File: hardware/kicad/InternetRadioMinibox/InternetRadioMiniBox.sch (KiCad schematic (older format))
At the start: 59 parts, among them IC1 ESP8266, IC2 ATMEGA328P-P, IC3 23K256, IC4 VS1011e, IC5 LM386, M1 TSR1-2433, M2 TSR1-2433, M3 TSR1-2433, P1 CONN_01X02, P2 CONN_01X02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

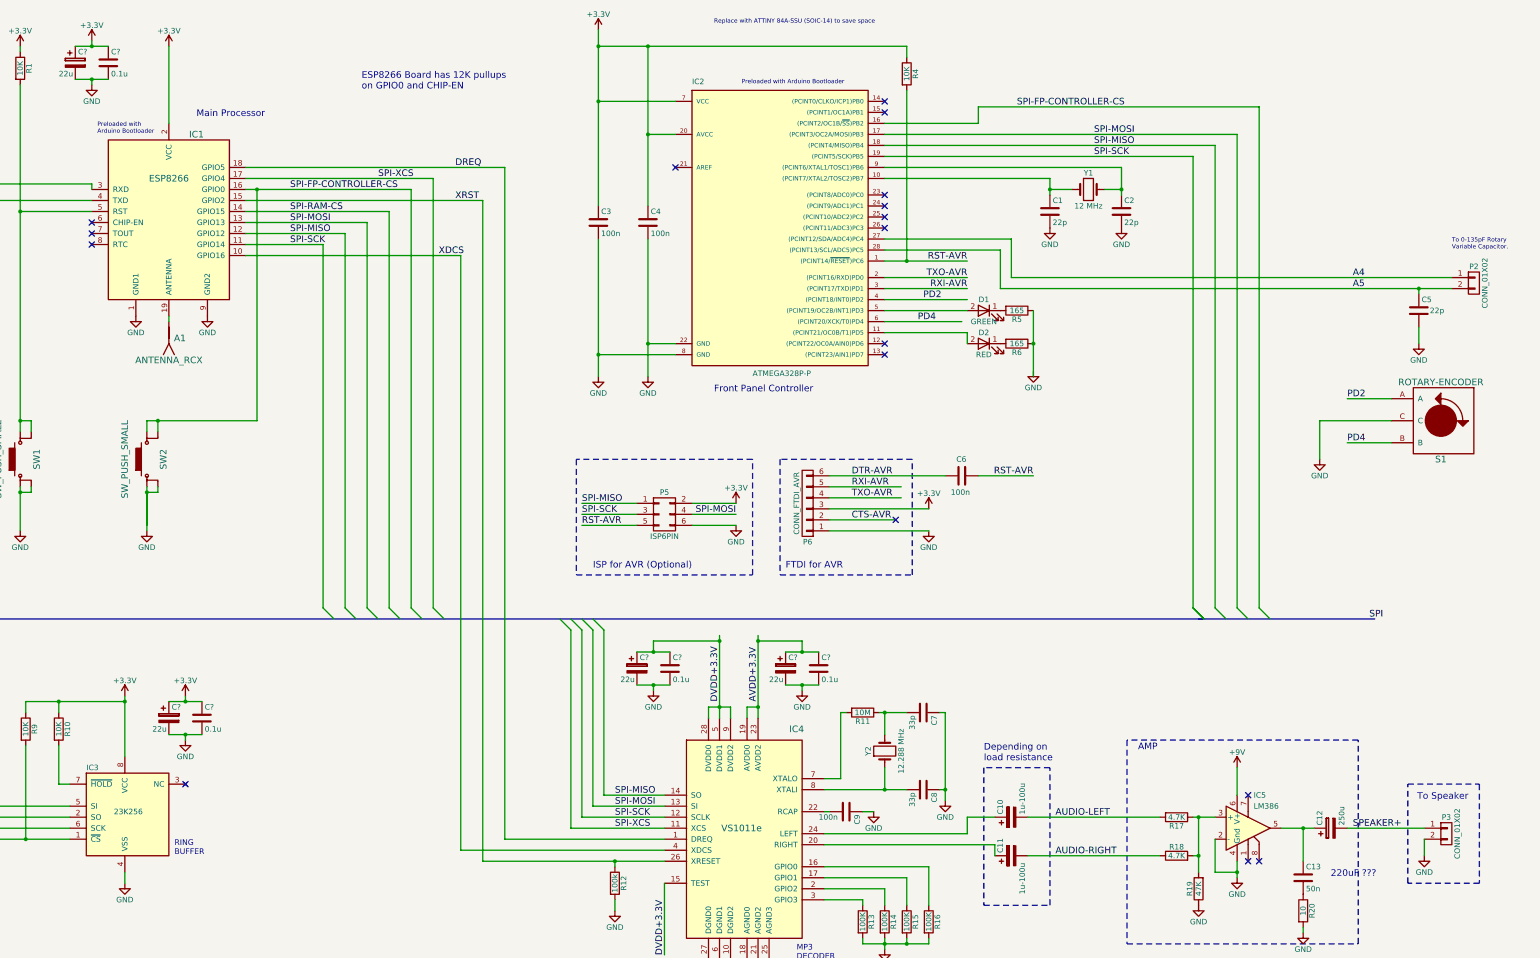
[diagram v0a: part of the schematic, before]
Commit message: Added control components and decoupling capacitors.
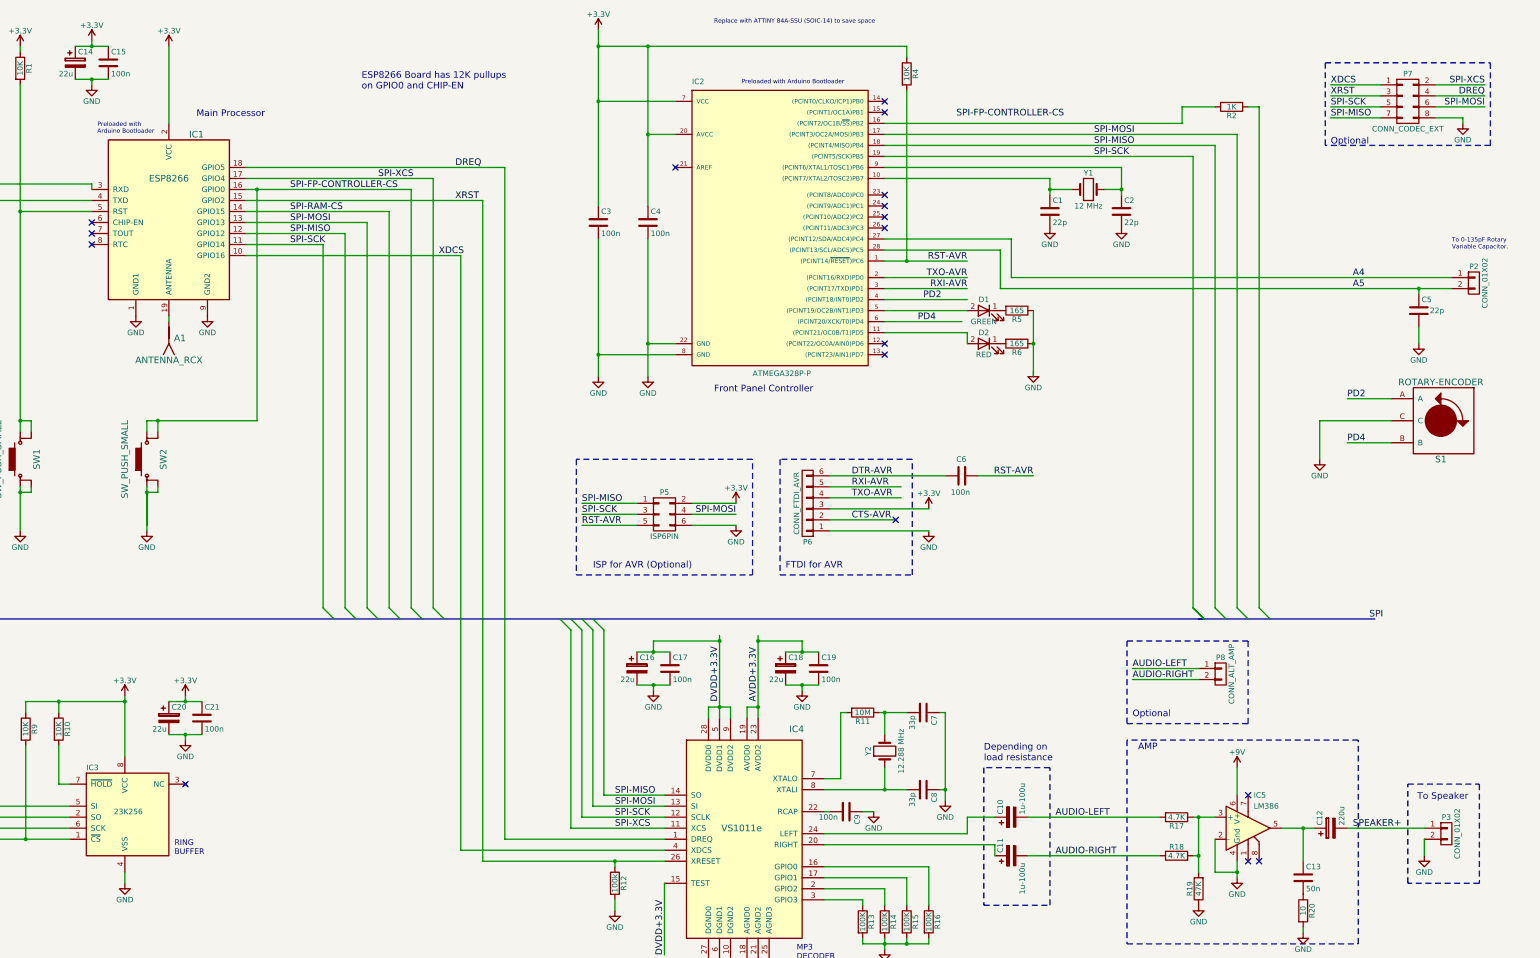
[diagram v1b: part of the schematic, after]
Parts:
- added P7: CONN_CODEC_EXT, maker:CONNECT_PINHEAD_2_4, symbol CONN_02X04
- added P8: CONN_ALT_AMP, Connect:PINHEAD1-2, symbol CONN_01X02
- added R2: 1K, Resistors_SMD:R_0805_HandSoldering, symbol R
- C12: value 250u -> 220u; footprint (none) -> maker:C_RADIAL_D8_P3.5
- C14, C16, C18, C20: renamed from C?; footprint (none) -> Capacitors_ThroughHole:CP_Radial_D5.0mm_P2.00mm
- C15, C17, C19, C21: renamed from C?; value 0.1u -> 100n; footprint (none) -> Capacitors_SMD:C_0805_HandSoldering
- D1, D2: footprint (none) -> LEDs:LED_1206
- P2: footprint (none) -> Connect:PINHEAD1-2
- P5: footprint (none) -> maker:CONNECT_PINHEAD_2_3
- P6: footprint (none) -> Connect:PINHEAD1-6
- S1: footprint (none) -> maker:ROTARY_ENCODER_EC12
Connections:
- wire segments 233 -> 245
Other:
- note added: "Optional"
- note removed: "220uF ???"
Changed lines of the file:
@@
 F 0 "D2" H 11100 3900 50  0000 C CNN
 F 1 "RED" H 11100 3700 50  0000 C CNN
-F 2 "" H 11100 3800 50  0001 C CNN
+F 2 "LEDs:LED_1206" H 11100 3800 50  0001 C CNN
 F 3 "" H 11100 3800 50  0000 C CNN
 	1    11100 3800
@@
 F 0 "D1" H 11100 3600 50  0000 C CNN
 F 1 "GREEN" H 11100 3400 50  0000 C CNN
-F 2 "" H 11100 3500 50  0001 C CNN
+F 2 "LEDs:LED_1206" H 11100 3500 50  0001 C CNN
 F 3 "" H 11100 3500 50  0000 C CNN
 	1    11100 3500
@@
 Text Notes 950  3000 0    60   ~ 0
 FTDI\nfor ESP8266
-Text Label 11400 1650 0    60   ~ 0
+Text Label 10850 1750 0    60   ~ 0
 SPI-FP-CONTROLLER-CS
 Text Notes 3050 1900 0    39   ~ 0
@@
 P 14250 8200
 F 0 "C12" H 14275 8300 50  0000 L CNN
-F 1 "250u" H 14275 8100 50  0000 L CNN
-F 2 "" H 14288 8050 50  0001 C CNN
+F 1 "220u" H 14275 8100 50  0000 L CNN
+F 2 "maker:C_RADIAL_D8_P3.5" H 14288 8050 50  0001 C CNN
 F 3 "" H 14250 8200 50  0000 C CNN
 	1    14250 8200
@@
 	10200 1900 13400 1900
 Wire Wire Line
-	10200 1800 11050 1800
+	10200 1800 12900 1800
 Wire Wire Line
 	11250 2950 11250 3300
@@
 	7350 6400 7350 8200
 Wire Wire Line
-	11050 1800 11050 1650
+	13200 1650 12900 1650
 Wire Wire Line
 	4400 2600 5700 2600
@@
 	13000 2100 13000 6200
 Wire Wire Line
-	11050 1650 13600 1650
+	13500 1650 13600 1650
 Wire Wire Line
 	2400 7050 2400 7150
@@
 F 0 "P5" H 8200 5550 50  0000 C CNN
 F 1 "ISP6PIN" H 8200 5150 50  0000 C CNN
-F 2 "" H 8200 4150 50  0001 C CNN
+F 2 "maker:CONNECT_PINHEAD_2_3" H 8200 4150 50  0001 C CNN
 F 3 "" H 8200 4150 50  0000 C CNN
 	1    8200 5350
@@
 F 0 "P6" H 9500 5600 50  0000 C CNN
 F 1 "CONN_FTDI_AVR" V 9600 5250 50  0000 C CNN
-F 2 "" H 9500 5250 50  0001 C CNN
+F 2 "Connect:PINHEAD1-6" H 9500 5250 50  0001 C CNN
 F 3 "" H 9500 5250 50  0000 C CNN
 	1    9500 5250
@@
 F 0 "S1" V 15600 4500 60  0000 C CNN
 F 1 "ROTARY-ENCODER" V 14900 4500 60  0000 C CNN
-F 2 "" H 15250 4500 60  0001 C CNN
+F 2 "maker:ROTARY_ENCODER_EC12" H 15250 4500 60  0001 C CNN
 F 3 "" H 15250 4500 60  0001 C CNN
 	1    15250 4500
@@
 F 0 "P2" H 15550 3400 50  0000 C CNN
 F 1 "CONN_01X02" V 15650 3250 50  0000 C CNN
-F 2 "" H 15550 3250 50  0001 C CNN
+F 2 "Connect:PINHEAD1-2" H 15550 3250 50  0001 C CNN
 F 3 "" H 15550 3250 50  0000 C CNN
 	1    15550 3250
@@
 $EndComp
 NoConn ~ 10200 2450
-Text Notes 14250 8650 0    60   ~ 0
-220uF ???
-$Comp
-L CP C?
+$Comp
+L CP C14
 U 1 1 5905CE91
 P 2850 1250
-F 0 "C?" H 2875 1350 50  0000 L CNN
+F 0 "C14" H 2875 1350 50  0000 L CNN
 F 1 "22u" H 2700 1150 50  0000 L CNN
-F 2 "" H 2888 1100 50  0000 C CNN
+F 2 "Capacitors_ThroughHole:CP_Radial_D5.0mm_P2.00mm" H 2888 1100 50  0001 C CNN
 F 3 "" H 2850 1250 50  0000 C CNN
 	1    2850 1250
@@
 $EndComp
 $Comp
-L C C?
+L C C15
 U 1 1 5905CF1A
 P 3150 1250
-F 0 "C?" H 3175 1350 50  0000 L CNN
-F 1 "0.1u" H 3175 1150 50  0000 L CNN
-F 2 "" H 3188 1100 50  0000 C CNN
+F 0 "C15" H 3175 1350 50  0000 L CNN
+F 1 "100n" H 3175 1150 50  0000 L CNN
+F 2 "Capacitors_SMD:C_0805_HandSoldering" H 3188 1100 50  0001 C CNN
 F 3 "" H 3150 1250 50  0000 C CNN
 	1    3150 1250
@@
 	2850 1400 3150 1400
 $Comp
-L +3.3V #PWR?
+L +3.3V #PWR044
 U 1 1 5905E727
 P 3000 1050
-F 0 "#PWR?" H 3000 900 50  0001 C CNN
+F 0 "#PWR044" H 3000 900 50  0001 C CNN
 F 1 "+3.3V" H 3000 1190 50  0000 C CNN
 F 2 "" H 3000 1050 50  0000 C CNN
@@
 $EndComp
 $Comp
-L GND #PWR?
+L GND #PWR045
 U 1 1 5905E7A5
 P 3000 1450
-F 0 "#PWR?" H 3000 1200 50  0001 C CNN
+F 0 "#PWR045" H 3000 1200 50  0001 C CNN
 F 1 "GND" H 3000 1300 50  0000 C CNN
 F 2 "" H 3000 1450 50  0000 C CNN
@@
 Connection ~ 3000 1400
 $Comp
-L CP C?
+L CP C20
 U 1 1 59060BA4
 P 3700 7200
-F 0 "C?" H 3725 7300 50  0000 L CNN
+F 0 "C20" H 3725 7300 50  0000 L CNN
 F 1 "22u" H 3550 7100 50  0000 L CNN
-F 2 "" H 3738 7050 50  0000 C CNN
+F 2 "Capacitors_ThroughHole:CP_Radial_D5.0mm_P2.00mm" H 3738 7050 50  0001 C CNN
 F 3 "" H 3700 7200 50  0000 C CNN
 	1    3700 7200
@@
 $EndComp
 $Comp
-L C C?
+L C C21
 U 1 1 59060BAA
 P 4000 7200
-F 0 "C?" H 4025 7300 50  0000 L CNN
-F 1 "0.1u" H 4025 7100 50  0000 L CNN
-F 2 "" H 4038 7050 50  0000 C CNN
+F 0 "C21" H 4025 7300 50  0000 L CNN
+F 1 "100n" H 4025 7100 50  0000 L CNN
+F 2 "Capacitors_SMD:C_0805_HandSoldering" H 4038 7050 50  0001 C CNN
 F 3 "" H 4000 7200 50  0000 C CNN
 	1    4000 7200
@@
 	3700 7350 4000 7350
 $Comp
-L +3.3V #PWR?
+L +3.3V #PWR046
 U 1 1 59060BB4
 P 3850 7000
-F 0 "#PWR?" H 3850 6850 50  0001 C CNN
+F 0 "#PWR046" H 3850 6850 50  0001 C CNN
 F 1 "+3.3V" H 3850 7140 50  0000 C CNN
 F 2 "" H 3850 7000 50  0000 C CNN
@@
 $EndComp
 $Comp
-L GND #PWR?
+L GND #PWR047
 U 1 1 59060BBA
 P 3850 7400
-F 0 "#PWR?" H 3850 7150 50  0001 C CNN
+F 0 "#PWR047" H 3850 7150 50  0001 C CNN
 F 1 "GND" H 3850 7250 50  0000 C CNN
 F 2 "" H 3850 7400 50  0000 C CNN
@@
 Connection ~ 3850 7350
 $Comp
-L CP C?
+L CP C16
 U 1 1 59062737
 P 7950 6750
-F 0 "C?" H 7975 6850 50  0000 L CNN
+F 0 "C16" H 7975 6850 50  0000 L CNN
 F 1 "22u" H 7800 6650 50  0000 L CNN
-F 2 "" H 7988 6600 50  0000 C CNN
+F 2 "Capacitors_ThroughHole:CP_Radial_D5.0mm_P2.00mm" H 7988 6600 50  0001 C CNN
 F 3 "" H 7950 6750 50  0000 C CNN
 	1    7950 6750
@@
 $EndComp
 $Comp
-L C C?
+L C C17
 U 1 1 5906273D
 P 8250 6750
-F 0 "C?" H 8275 6850 50  0000 L CNN
-F 1 "0.1u" H 8275 6650 50  0000 L CNN
-F 2 "" H 8288 6600 50  0000 C CNN
+F 0 "C17" H 8275 6850 50  0000 L CNN
+F 1 "100n" H 8275 6650 50  0000 L CNN
+F 2 "Capacitors_SMD:C_0805_HandSoldering" H 8288 6600 50  0001 C CNN
 F 3 "" H 8250 6750 50  0000 C CNN
 	1    8250 6750
@@
 	7950 6900 8250 6900
 $Comp
-L GND #PWR?
+L GND #PWR048
 U 1 1 5906274D
 P 8100 6950
-F 0 "#PWR?" H 8100 6700 50  0001 C CNN
+F 0 "#PWR048" H 8100 6700 50  0001 C CNN
 F 1 "GND" H 8100 6800 50  0000 C CNN
 F 2 "" H 8100 6950 50  0000 C CNN
@@
 Connection ~ 8100 6900
 $Comp
-L CP C?
+L CP C18
 U 1 1 59062D0E
 P 9300 6750
-F 0 "C?" H 9325 6850 50  0000 L CNN
+F 0 "C18" H 9325 6850 50  0000 L CNN
 F 1 "22u" H 9150 6650 50  0000 L CNN
-F 2 "" H 9338 6600 50  0000 C CNN
+F 2 "Capacitors_ThroughHole:CP_Radial_D5.0mm_P2.00mm" H 9338 6600 50  0001 C CNN
 F 3 "" H 9300 6750 50  0000 C CNN
 	1    9300 6750
@@
 $EndComp
 $Comp
-L C C?
+L C C19
 U 1 1 59062D14
 P 9600 6750
-F 0 "C?" H 9625 6850 50  0000 L CNN
-F 1 "0.1u" H 9625 6650 50  0000 L CNN
-F 2 "" H 9638 6600 50  0000 C CNN
+F 0 "C19" H 9625 6850 50  0000 L CNN
+F 1 "100n" H 9625 6650 50  0000 L CNN
+F 2 "Capacitors_SMD:C_0805_HandSoldering" H 9638 6600 50  0001 C CNN
 F 3 "" H 9600 6750 50  0000 C CNN
 	1    9600 6750
@@
 	9300 6900 9600 6900
 $Comp
-L GND #PWR?
+L GND #PWR049
 U 1 1 59062D24
 P 9450 6950
-F 0 "#PWR?" H 9450 6700 50  0001 C CNN
+F 0 "#PWR049" H 9450 6700 50  0001 C CNN
 F 1 "GND" H 9450 6800 50  0000 C CNN
 F 2 "" H 9450 6950 50  0000 C CNN
@@
 	9450 6500 9050 6500
 Connection ~ 9050 6500
+$Comp
+L CONN_02X04 P7
+U 1 1 5906D80C
+P 14950 1600
+F 0 "P7" H 14950 1850 50  0000 C CNN
+F 1 "CONN_CODEC_EXT" H 14950 1350 50  0000 C CNN
+F 2 "maker:CONNECT_PINHEAD_2_4" H 14950 400 50  0001 C CNN
+F 3 "" H 14950 400 50  0000 C CNN
+	1    14950 1600
+	1    0    0    -1
+$EndComp
+Wire Wire Line
+	14700 1450 14250 1450
+Text Label 14250 1450 0    60   ~ 0
+XDCS
+Wire Wire Line
+	14700 1550 14250 1550
+Wire Wire Line
+	14700 1650 14250 1650
+Wire Wire Line
+	14700 1750 14250 1750
+Wire Wire Line
+	15200 1750 15450 1750
+Wire Wire Line
+	15200 1650 15650 1650
+Wire Wire Line
+	15200 1550 15650 1550
+Wire Wire Line
+	15200 1450 15650 1450
+Text Label 14250 1550 0    60   ~ 0
+XRST
+Text Label 14250 1650 0    60   ~ 0
+SPI-SCK
+Text Label 14250 1750 0    60   ~ 0
+SPI-MISO
+Text Label 15650 1450 2    60   ~ 0
+SPI-XCS
+Text Label 15650 1550 2    60   ~ 0
+DREQ
+Text Label 15650 1650 2    60   ~ 0
+SPI-MOSI
+$Comp
+L GND #PWR050
+U 1 1 5907192F
+P 15450 1800
+F 0 "#PWR050" H 15450 1550 50  0001 C CNN
+F 1 "GND" H 15450 1650 50  0000 C CNN
+F 2 "" H 15450 1800 50  0000 C CNN
+F 3 "" H 15450 1800 50  0000 C CNN
+	1    15450 1800
+	1    0    0    -1
+$EndComp
+Wire Wire Line
+	15450 1750 15450 1800
+Wire Notes Line
+	14200 1250 15700 1250
+Wire Notes Line
+	15700 1250 15700 2000
+Wire Notes Line
+	15700 2000 14200 2000
+Wire Notes Line
+	14200 2000 14200 1250
+Text Notes 14250 2000 0    60   ~ 0
+Optional
+$Comp
+L CONN_01X02 P8
+U 1 1 59091002
+P 13250 6800
+F 0 "P8" H 13250 6950 50  0000 C CNN
+F 1 "CONN_ALT_AMP" V 13350 6800 50  0000 C CNN
+F 2 "Connect:PINHEAD1-2" H 13250 6800 50  0001 C CNN
+F 3 "" H 13250 6800 50  0000 C CNN
+	1    13250 6800
+	1    0    0    -1
+$EndComp
+Wire Wire Line
+	12450 6750 13050 6750
+Wire Wire Line
+	13050 6850 12450 6850
+Text Label 12450 6750 0    60   ~ 0
+AUDIO-LEFT
+Text Label 12450 6850 0    60   ~ 0
+AUDIO-RIGHT
+Wire Notes Line
+	12400 6500 13500 6500
+Wire Notes Line
+	13500 6500 13500 7250
+Wire Notes Line
+	13500 7250 12400 7250
+Wire Notes Line
+	12400 7250 12400 6500
+Text Notes 12450 7200 0    60   ~ 0
+Optional
+$Comp
+L R R2
+U 1 1 59C64AE7
+P 13350 1650
+F 0 "R2" V 13430 1650 50  0000 C CNN
+F 1 "1K" V 13350 1650 50  0000 C CNN
+F 2 "Resistors_SMD:R_0805_HandSoldering" V 13280 1650 50  0001 C CNN
+F 3 "" H 13350 1650 50  0000 C CNN
+	1    13350 1650
+	0    1    1    0
+$EndComp
+Wire Wire Line
+	12900 1650 12900 1800
 $EndSCHEMATC

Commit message: Added CS decoder logic and interrupt line from front panel controller
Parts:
- removed R2: 1K, Resistors_SMD:R_0805_HandSoldering, symbol R
- added U1: 74HC00, symbol 74HC00
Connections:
- net labels added: FP-CHANGE-INTR
- wire segments 245 -> 317
- no-connect marks 19 -> 18
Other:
- note added: "CS Decoder\n"
- note added: "ESP8266 Board has 12K \npullups on GPIO0 and CHIP-EN"
- note added: "Program"
- note added: "Reset"
- note removed: "ESP8266 Board has 12K pullups \non GPIO0 and CHIP-EN"
- moved on the sheet: A1, SW2

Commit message: Brought the erronous integration2 branch to the branch master (this branch)
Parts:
- removed P7: CONN_CODEC_EXT, maker:CONNECT_PINHEAD_2_4, symbol CONN_02X04
- removed P8: CONN_ALT_AMP, Connect:PINHEAD1-2, symbol CONN_01X02
- removed U1: 74HC00, symbol 74HC00
- C12: value 220u -> 250u; footprint maker:C_RADIAL_D8_P3.5 -> (none)
- C?: renamed from C14; footprint Capacitors_ThroughHole:CP_Radial_D5.0mm_P2.00mm -> (none)
- C?: renamed from C15; value 100n -> 0.1u; footprint Capacitors_SMD:C_0805_HandSoldering -> (none)
- C?: renamed from C20; footprint Capacitors_ThroughHole:CP_Radial_D5.0mm_P2.00mm -> (none)
- C?: renamed from C21; value 100n -> 0.1u; footprint Capacitors_SMD:C_0805_HandSoldering -> (none)
- C?: renamed from C16; footprint Capacitors_ThroughHole:CP_Radial_D5.0mm_P2.00mm -> (none)
- C?: renamed from C17; value 100n -> 0.1u; footprint Capacitors_SMD:C_0805_HandSoldering -> (none)
- C?: renamed from C18; footprint Capacitors_ThroughHole:CP_Radial_D5.0mm_P2.00mm -> (none)
- C?: renamed from C19; value 100n -> 0.1u; footprint Capacitors_SMD:C_0805_HandSoldering -> (none)
- D1, D2: footprint LEDs:LED_1206 -> (none)
- P2: footprint Connect:PINHEAD1-2 -> (none)
- P5: footprint maker:CONNECT_PINHEAD_2_3 -> (none)
- P6: footprint Connect:PINHEAD1-6 -> (none)
- S1: footprint maker:ROTARY_ENCODER_EC12 -> (none)
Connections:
- net labels removed: FP-CHANGE-INTR
- wire segments 317 -> 233
- no-connect marks 18 -> 19
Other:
- note added: "220uF ???"
- note added: "ESP8266 Board has 12K pullups \non GPIO0 and CHIP-EN"
- note removed: "CS Decoder\n"
- note removed: "ESP8266 Board has 12K \npullups on GPIO0 and CHIP-EN"
- note removed: "Optional"
- note removed: "Program"
- note removed: "Reset"
- moved on the sheet: A1, SW2

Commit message: Brought the erronous master branch to the branch integration2 (this branch)
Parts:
- added P7: CONN_CODEC_EXT, maker:CONNECT_PINHEAD_2_4, symbol CONN_02X04
- added P8: CONN_ALT_AMP, Connect:PINHEAD1-2, symbol CONN_01X02
- added U1: 74HC00, symbol 74HC00
- C12: value 250u -> 220u; footprint (none) -> maker:C_RADIAL_D8_P3.5
- C14, C16, C18, C20: renamed from C?; footprint (none) -> Capacitors_ThroughHole:CP_Radial_D5.0mm_P2.00mm
- C15, C17, C19, C21: renamed from C?; value 0.1u -> 100n; footprint (none) -> Capacitors_SMD:C_0805_HandSoldering
- D1, D2: footprint (none) -> LEDs:LED_1206
- P2: footprint (none) -> Connect:PINHEAD1-2
- P5: footprint (none) -> maker:CONNECT_PINHEAD_2_3
- P6: footprint (none) -> Connect:PINHEAD1-6
- S1: footprint (none) -> maker:ROTARY_ENCODER_EC12
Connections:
- net labels added: FP-CHANGE-INTR
- wire segments 233 -> 317
- no-connect marks 19 -> 18
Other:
- note added: "CS Decoder\n"
- note added: "ESP8266 Board has 12K \npullups on GPIO0 and CHIP-EN"
- note added: "Optional"
- note added: "Program"
- note added: "Reset"
- note removed: "220uF ???"
- note removed: "ESP8266 Board has 12K pullups \non GPIO0 and CHIP-EN"
- moved on the sheet: A1, SW2
